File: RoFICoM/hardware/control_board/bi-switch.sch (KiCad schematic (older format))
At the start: 11 parts, among them Q1 DMP6050SFG, Q2 SSM3K72KCT, Q3 DMP6050SFG, U6 ACS70331

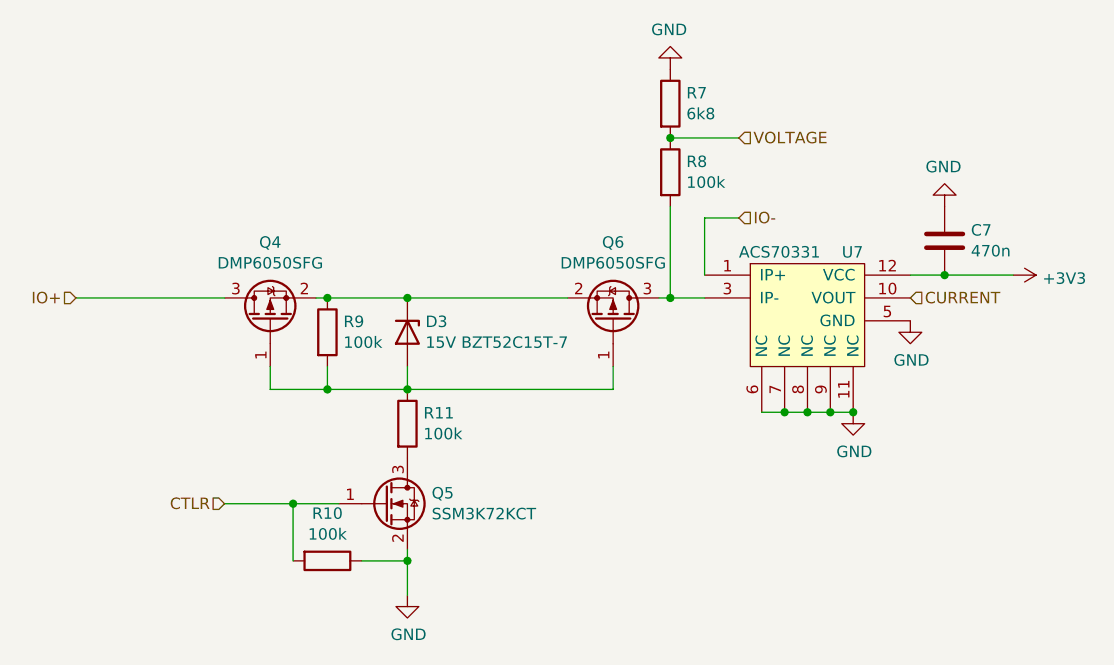
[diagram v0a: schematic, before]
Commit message: RoFICoM: Add new board revision
- change voltage regulator and switching transistors
- fix wrong wiring of SWD
- add Molex board-to-board connectors for system and debugging
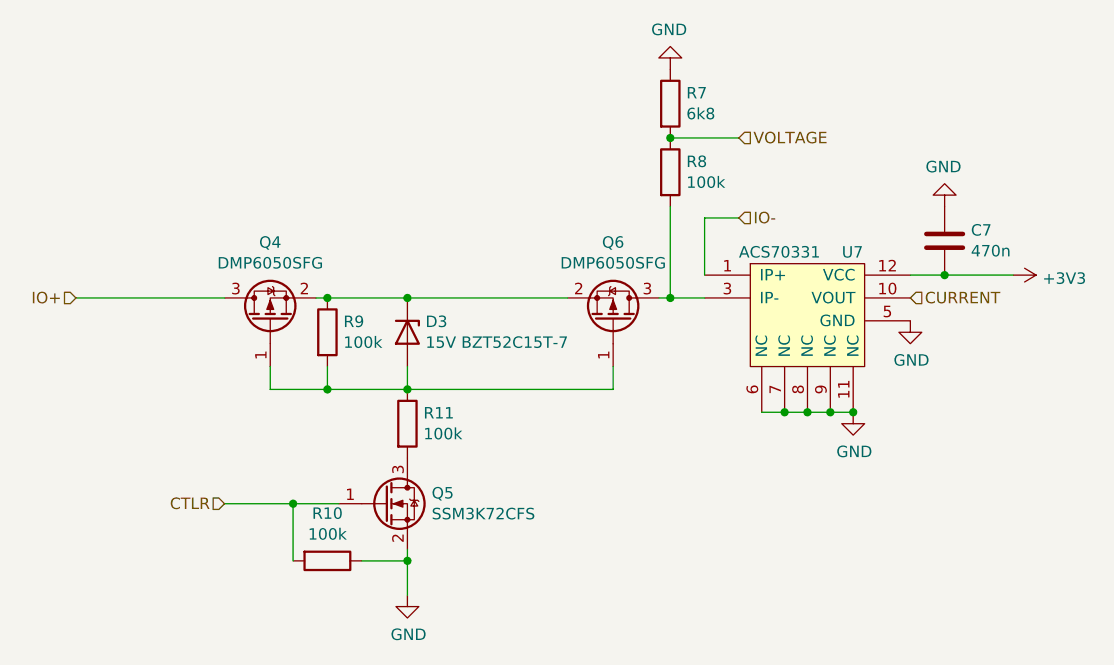
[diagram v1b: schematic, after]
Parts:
- Q2: value SSM3K72KCT -> SSM3K72CFS; footprint rofi:CST3 -> Package_TO_SOT_SMD:SOT-416; manf# (none) -> SSM3K72CFS,LF
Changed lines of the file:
@@
 EESchema Schematic File Version 4
 LIBS:control_board-cache
-EELAYER 26 0
+EELAYER 29 0
 EELAYER END
 $Descr A4 11693 8268
@@
 AR Path="/5C883562/5C87EAED" Ref="Q5"  Part="1"
 F 0 "Q5" H 4956 3946 50  0000 L CNN
-F 1 "SSM3K72KCT" H 4956 3855 50  0000 L CNN
-F 2 "rofi:CST3" H 4950 4000 50  0001 C CNN
+F 1 "SSM3K72CFS" H 4956 3855 50  0000 L CNN
+F 2 "Package_TO_SOT_SMD:SOT-416" H 4950 4000 50  0001 C CNN
 F 3 "~" H 4750 3900 50  0001 C CNN
+F 4 "SSM3K72CFS,LF" H 4750 3900 50  0001 C CNN "manf#"
 	1    4750 3900
 	1    0    0    -1
